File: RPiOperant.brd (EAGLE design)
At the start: 136 x 94 mm, 69 parts, among them IC1 74LS14N, IC2 74LS14N, J2 POWER_JACK

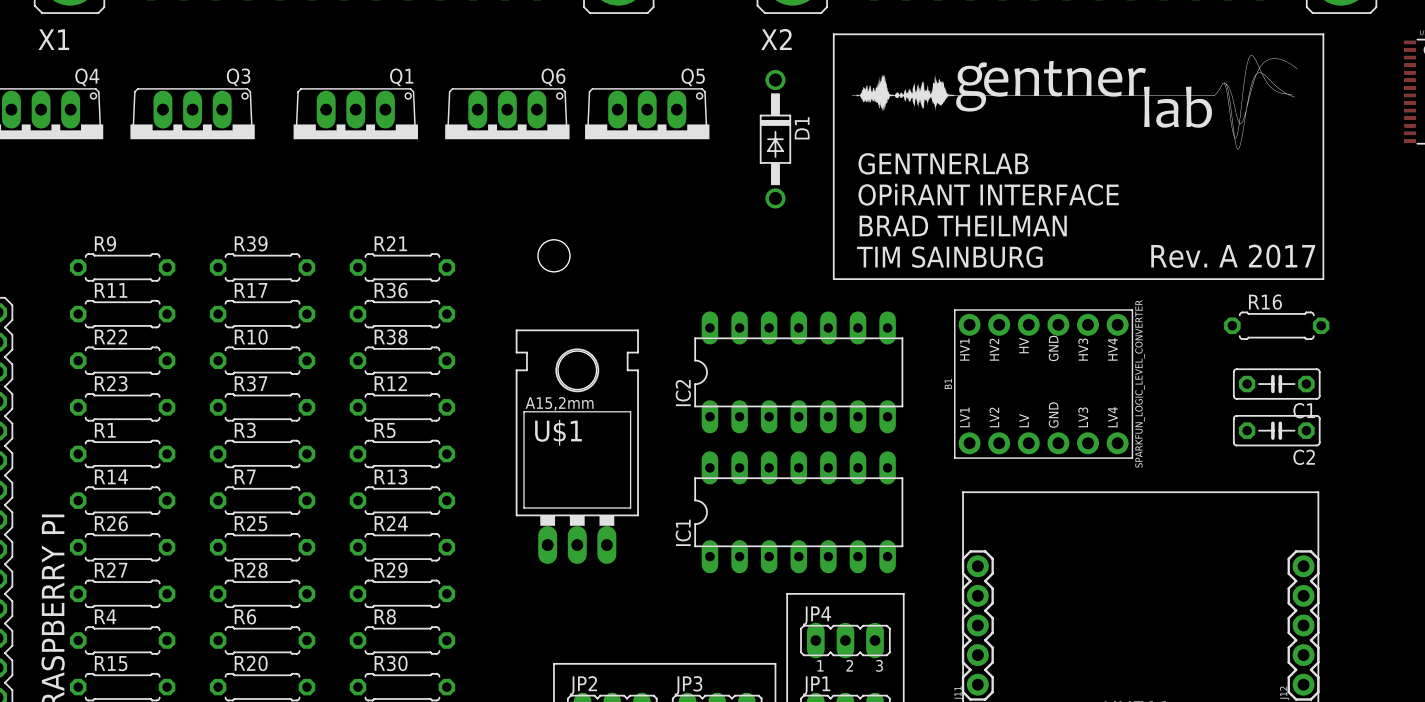
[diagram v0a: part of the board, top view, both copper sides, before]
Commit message: rev b changes... new DB25 pinout
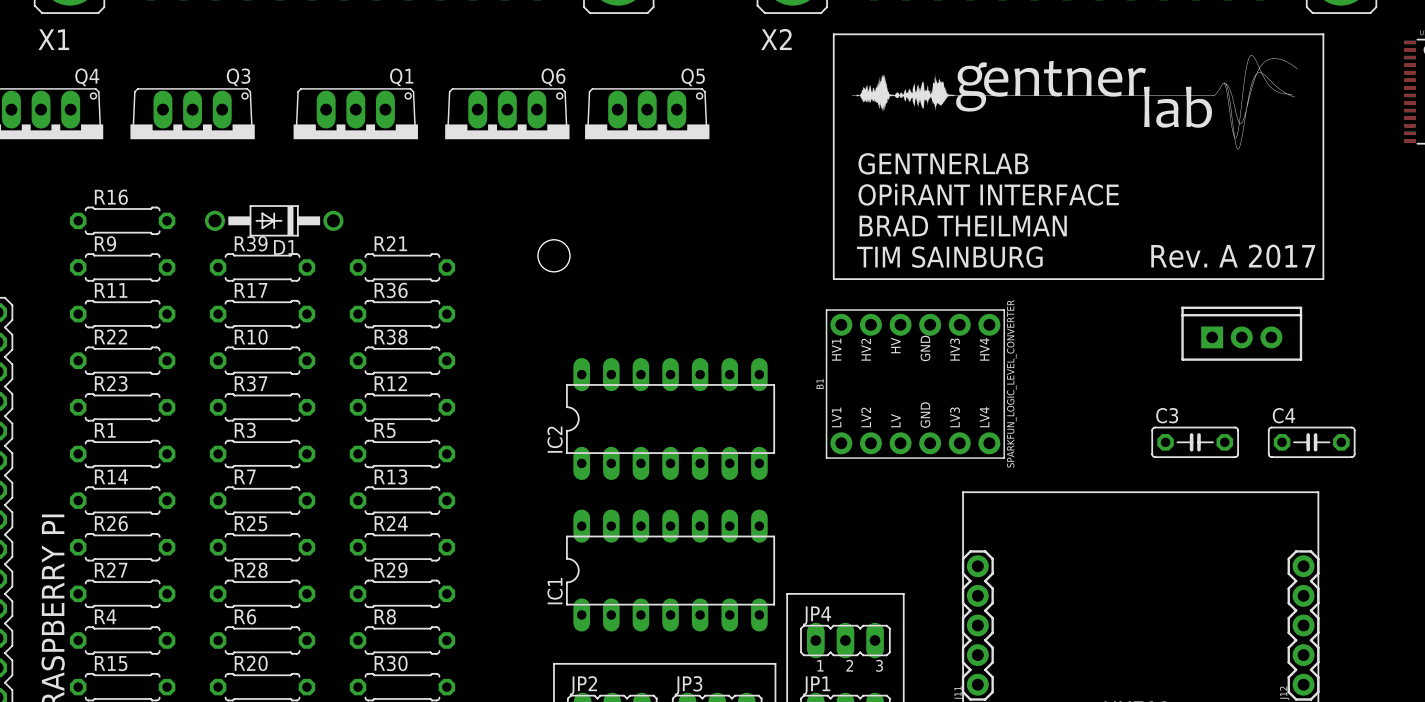
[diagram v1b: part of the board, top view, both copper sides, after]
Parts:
- removed C1: 100nF, adafruit:C050-025X075
- removed C2: 10uF, adafruit:C050-025X075
- removed U$1: V_REG_LD1117VXX, SparkFun-IC-Power:78XXL
- added C3: 100nF, adafruit:C050-025X075
- added C4: 10uF, adafruit:C050-025X075
- added U2: (no value), SparkFun-IC-Power:TO220-IGO
- moved R16 99.4 mm to (16.0, 65.0)
- moved D1 43.6 mm to (29.0, 65.0), turned to 180 degrees
- moved IC1 12.1 mm to (63.0, 35.0)
- moved IC2 11.7 mm to (63.0, 48.0)
- moved B1 11.0 mm to (84.0, 51.0)
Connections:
- net +3V3: now also C4.1, U2.OUT, X1.2; no longer C2.1, U$1.GND
- net 12V: now also C3.1, U2.IN, X1.1; no longer C1.1, U$1.OUT
- net GND: now also C3.2, C4.2, U2.GND; no longer C1.2, C2.2, U$1.IN
- net TTL22: no longer X1.2
- net TTL27: no longer X1.1

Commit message: new board layout
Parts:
- moved C4 107.7 mm to (14.0, 18.0), turned to 90 degrees
- moved C3 92.3 mm to (20.0, 18.0), turned to 90 degrees
- moved U2 85.0 mm to (36.0, 17.0)
- moved R1 79.0 mm to (95.0, 47.0)
- moved R10 79.0 mm to (107.0, 55.0)
- moved R11 79.0 mm to (95.0, 59.0)
- moved R12 79.0 mm to (119.0, 51.0)
- moved R13 79.0 mm to (119.0, 43.0)
- moved R14 79.0 mm to (95.0, 43.0)
- moved R15 79.0 mm to (95.0, 27.0)
- moved R17 79.0 mm to (107.0, 59.0)
- moved R2 79.0 mm to (95.0, 19.0)
- moved R20 79.0 mm to (107.0, 27.0)
- moved R21 79.0 mm to (119.0, 63.0)
- moved R22 79.0 mm to (95.0, 55.0)
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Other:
- board text added: "Rev. B 2018"
- board text removed: "3.3V 5V"
- board text removed: "5 V"
- board text removed: "GPIO LC"
- board text removed: "LOAD CELL SELECT"
- board text removed: "Rev. A 2017"
- board text removed: "TTL SELECT"

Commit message: revb revisions
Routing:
- net GND: track 0.00 -> 590.5 mm, vias 0 -> 6
- net 12V: track 0.00 -> 393.1 mm, vias 0 -> 4
- net +3V3: track 0.00 -> 347.9 mm, vias 0 -> 11
- net AUX2: track 0.00 -> 259.7 mm, vias 0 -> 9
- net GPIO7: track 0.00 -> 255.2 mm, vias 0 -> 2
- net RIGHT_PECK_GPIO: track 0.00 -> 243.1 mm, vias 0 -> 5
- net CENTER_PECK_GPIO: track 0.00 -> 233.9 mm, vias 0 -> 7
- net GPIO22: track 0.00 -> 223.7 mm, vias 0 -> 7
- net IR_5_GPIO: track 0.00 -> 221.8 mm, vias 0 -> 3
- net TXD: track 0.00 -> 213.0 mm, vias 0 -> 16
- net RXD: track 0.00 -> 207.8 mm, vias 0 -> 3
- net LEFT_PECK_GPIO: track 0.00 -> 199.9 mm, vias 0 -> 5
- net RPI_3.3V: track 0.00 -> 197.2 mm, vias 0 -> 7
- net HOPPER_IR_GPIO: track 0.00 -> 196.0 mm, vias 0 -> 4
- net SCL: track 0.00 -> 195.5 mm, vias 0 -> 4
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
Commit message: new board!
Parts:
- removed J1: (no value), SparkFun-Connectors:SCREWTERMINAL-3.5MM-4
- removed J10, J13, J14: (no value), SparkFun-Connectors:SCREWTERMINAL-3.5MM-3
- removed J15, J9: (no value), SparkFun-Connectors:SCREWTERMINAL-3.5MM-2
- removed X2: (no value), con-subd:F25HP
- added X3: 2550-, con-3m:PAK100/2500-50
- X1: value (none) -> 2516-; device con-subd:F25HP -> con-3m:PAK100/2500-16
- moved X1 80.8 mm to (41.5, 5.50)
- moved C3 64.0 mm to (19.0, 82.0), turned to 180 degrees
- moved U2 63.8 mm to (10.5, 75.5), turned to 270 degrees
- moved R38 58.6 mm to (64.5, 76.5), turned to 270 degrees
- moved B1 54.8 mm to (98.0, 8.00)
- moved R36 51.6 mm to (70.5, 76.5), turned to 270 degrees
- moved R13 51.3 mm to (72.0, 22.5), turned to 90 degrees
- moved R16 49.9 mm to (32.0, 51.5)
- moved C4 49.8 mm to (19.0, 67.5), turned to 180 degrees
- moved R12 49.6 mm to (76.5, 76.5), turned to 270 degrees
- moved R37 47.0 mm to (67.5, 76.5), turned to 270 degrees
- moved D1 44.8 mm to (33.0, 57.0), turned to 0 degrees
- moved J7 44.5 mm to (76.5, 3.00)
- moved J8 44.5 mm to (87.5, 3.00)
- moved R5 44.0 mm to (75.0, 46.5), turned to 270 degrees
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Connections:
- removed net N$32: J13.1, JP1.1
- removed net N$33: J13.2, JP4.1
- new net GPIO17EXT: JP1.1, X1.9
- new net GPIO8EXT: JP4.1, X1.10
- new net RGB_CUE_B\: X3.4
- net +3V3: now also X3.2; no longer X1.2
- net 12V: now also X3.1, X3.23; no longer X1.1, X1.23
- net AUX1: now also X1.1, X3.26; no longer J9.1, X2.1
- net AUX2: now also X1.2, X3.27; no longer J9.2, X2.2
- net AUX3: now also X1.3, X3.28; no longer J15.1, X2.3
- net AUX4: now also X1.4, X3.29; no longer J15.2, X2.4
- net AUX5: now also X1.5, X3.30; no longer J1.1, X2.5
- net AUX6: now also X1.6, X3.31; no longer J1.2, X2.6
- net AUX7: now also X1.7, X3.32; no longer J1.3, X2.7
- net AUX8: now also X1.8, X3.39; no longer J1.4, X2.14
- net CENTER_IR: now also X3.11; no longer X1.11
- net CENTER_LED: now also X3.8; no longer X1.8
- net GND: now also X1.15, X1.16; no longer J10.3, J13.3, J14.3, X1.G1, X1.G2, X2.G1, X2.G2
- net HOPPER: now also X3.6; no longer X1.6
- net HOPPER_IR: now also X3.13; no longer X1.13
- net HOUSELIGHT_B: now also X3.20; no longer X1.20
- net HOUSELIGHT_G: now also X3.21; no longer X1.21
- net HOUSELIGHT_R: now also X3.22; no longer X1.22
- net HOUSELIGHT_W: now also X3.19; no longer X1.19
- net IR_1: now also X3.50; no longer X2.25
- net IR_2: now also X3.49; no longer X2.24
- net IR_3: now also X3.48; no longer X2.23
- net IR_4: now also X3.47; no longer X2.22
- net IR_5: now also X3.46; no longer X2.21
- net IR_6: now also X3.45; no longer X2.20
- net LED_1: now also X3.38; no longer X2.13
- net LED_2: now also X3.37; no longer X2.12
- net LED_3: now also X3.36; no longer X2.11
- net LED_4: now also X3.35; no longer X2.10
- net LED_5: now also X3.34; no longer X2.9
- net LED_6: now also X3.33; no longer X2.8
- net LEFT_IR: now also X3.12; no longer X1.12
- net LEFT_LED: now also X3.9; no longer X1.9
- net LOADCELL2A+: now also X3.41; no longer X2.16
- net LOADCELL2A-: now also X3.40; no longer X2.15
- net LOADCELLA+: now also X3.15; no longer X1.15
- net LOADCELLA-: now also X3.14; no longer X1.14
- net LOADCELLE+: now also X3.25; no longer X1.25
- net LOADCELLE-: now also X3.24; no longer X1.24
- net RGB_CUE_B: no longer X1.4
- net RGB_CUE_G: now also X3.3; no longer X1.3
- net RGB_CUE_R: now also X3.5; no longer X1.5
- net RIGHT_IR: now also X3.10; no longer X1.10
- net RIGHT_LED: now also X3.7; no longer X1.7
- net RXD: now also X1.14; no longer J14.2
- net TTL22: now also X1.12; no longer J10.2
- net TTL27: now also X1.11; no longer J10.1
- net TXD: now also X1.13; no longer J14.1
- net USB1_D+: now also X3.16; no longer X1.16
- net USB1_D-: now also X3.17; no longer X1.17
- net USB1_VBUS: now also X3.18; no longer X1.18
- net USB2_D+: now also X3.42; no longer X2.17
- net USB2_D-: now also X3.43; no longer X2.18
- net USB2_VBUS: now also X3.44; no longer X2.19
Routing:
- net 12V: track 393.1 -> 165.0 mm, vias 4 -> 2
- net PCM_CLK: track 0.00 -> 168.9 mm, vias 0 -> 5
- net ID_SD: track 0.00 -> 149.3 mm, vias 0 -> 6
- net GPIO27: track 71.8 -> 201.3 mm, vias 2 -> 13
- net PCM_DIN: track 0.00 -> 128.8 mm, vias 0 -> 7
- net PCM_DOUT: track 0.00 -> 115.3 mm, vias 0 -> 2
- net GND: track 590.5 -> 475.2 mm, vias 6 -> 13
- net CENTER_PECK_GPIO: track 233.9 -> 132.7 mm, vias 7 -> 9
- net RXD: track 207.8 -> 308.8 mm, vias 3 -> 6
- net GPIO7: track 255.2 -> 161.4 mm, vias 2 -> 5
- net RGB_CUE_B: track 91.1 -> 0.00 mm, vias 3 -> 0
- net N$3: track 94.3 -> 5.09 mm, vias 2 -> 0
- net N$32: track 87.2 -> 0.00 mm, vias 3 -> 0
- net IR_3_GPIO: track 170.4 -> 251.6 mm, vias 9 -> 10
- net IR_5_GPIO: track 221.8 -> 140.6 mm, vias 3 -> 7
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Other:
- board size 136 x 94 mm -> 120 x 94 mm
- board text added: "+3.3V REGULATOR"
- board text added: "B"
- board text added: "Front Panel AUX"
- board text added: "G"
- board text added: "HOPPER"
- board text added: "HOUSELIGHTS"
- board text added: "IR Sensors"
- board text added: "LC SELECT EX LC"
- board text added: "LED CONTROL"
- board text added: "PCA9685"
- board text added: "PyOperant Interface Brad Theilman Tim Sainburg"
- board text added: "R"
- board text added: "TTL SELECT 3.3 5"
- board text added: "W"
- board text removed: "AUX1"
- board text removed: "AUX2"
- board text removed: "AUX3"
- board text removed: "AUX4"
- board text removed: "AUX5"
- board text removed: "AUX6"
- board text removed: "AUX7"
- board text removed: "AUX8"
- board text removed: "GENTNERLAB OPiRANT INTERFACE BRAD THEILMAN TIM SAINBURG"
- board text removed: "GND"
- board text removed: "GPIO17"
- board text removed: "GPIO8"
- board text removed: "RXD"
- board text removed: "TTL22"
- board text removed: "TTL27"
- board text removed: "TXD"

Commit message: new board
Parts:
- moved JP3 35.6 mm to (31.0, 43.5), turned to 90 degrees
- moved JP2 35.5 mm to (26.0, 43.5), turned to 90 degrees
- moved B1 31.4 mm to (67.5, 15.5)
- moved J11 25.8 mm to (50.0, 19.0), turned to 180 degrees
- moved J12 16.3 mm to (50.0, 46.9), turned to 180 degrees
- moved IC1 9.22 mm to (70.0, 41.0)
- moved IC2 9.22 mm to (90.5, 41.0)
- moved R1 9.22 mm to (62.0, 52.5)
- moved R13 9.22 mm to (65.0, 28.5)
- moved R14 9.22 mm to (68.0, 28.5)
- moved R15 9.22 mm to (74.0, 28.5)
- moved R2 9.22 mm to (77.0, 52.5)
- moved R20 9.22 mm to (71.0, 28.5)
- moved R24 9.22 mm to (82.5, 52.5)
- moved R25 9.22 mm to (85.5, 52.5)
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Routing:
- net RXD: track 308.8 -> 148.5 mm
- net LEFT_PECK_GPIO: track 203.8 -> 133.7 mm, vias 13 -> 6
- net IR_3_GPIO: track 251.6 -> 183.5 mm, vias 10 -> 6
- net GPIO27: track 201.3 -> 139.4 mm, vias 13 -> 5
- net USB1_D+: track 173.2 -> 116.9 mm, vias 4 -> 3
- net IR_6: track 138.8 -> 84.1 mm
- net HOUSELIGHT_B_GPIO: track 81.8 -> 130.1 mm, vias 5 -> 2
- net TTL22: track 12.5 -> 56.0 mm
- net IR_4_GPIO: track 134.5 -> 177.4 mm
- net AUX2: track 283.5 -> 243.6 mm, vias 6 -> 5
- net RPI_5V: track 193.7 -> 154.6 mm, vias 7 -> 5
- net GPIO22: track 191.3 -> 155.8 mm, vias 12 -> 4
- net AUX1: track 159.3 -> 124.5 mm
- net SCL: track 182.9 -> 148.9 mm, vias 5 -> 4
- net HOPPER_IR_GPIO: track 177.1 -> 144.3 mm, vias 8 -> 5
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
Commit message: rev_b layout
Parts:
- added R18, R19: 330, resistor:0207/7
- added X2: 22-23-2041, con-molex:22-23-2041
- moved C4 11.0 mm to (19.0, 78.5)
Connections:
- new net N$25: R19.1, X2.2
- new net N$31: R18.1, X2.3
- net +3V3: now also R19.2
- net GND: now also X2.1, X2.4
- net RPI_3.3V: now also R18.2
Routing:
- net USB1_D-: track 112.3 -> 218.9 mm, vias 7 -> 4
- net ID_SC: track 145.9 -> 234.8 mm, vias 6 -> 2
- net PCM_CLK: track 199.1 -> 111.9 mm, vias 2 -> 4
- net IR_1: track 93.4 -> 173.0 mm
- net GPIO27: track 139.4 -> 217.8 mm, vias 5 -> 3
- net USB1_D+: track 116.9 -> 189.9 mm
- net LOADCELLE+: track 78.7 -> 131.6 mm, vias 3 -> 2
- net IR_5_GPIO: track 171.9 -> 126.3 mm, vias 2 -> 4
- net GND: track 488.8 -> 443.3 mm, vias 9 -> 3
- net PCM_DOUT: track 142.9 -> 99.1 mm, vias 5 -> 0
- net IR_4_GPIO: track 177.4 -> 134.2 mm, vias 6 -> 4
- net IR_3_GPIO: track 183.5 -> 140.6 mm, vias 6 -> 4
- net USB1_VBUS: track 158.5 -> 118.8 mm, vias 4 -> 8
- net SDA: track 177.9 -> 139.1 mm, vias 2 -> 7
- net AUX2: track 243.6 -> 207.8 mm, vias 5 -> 6
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
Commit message: revb
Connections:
- removed net CENTNER_LED: R36.1
- removed net RGB_CUE_B\: X3.4
- net CENTER_LED: now also R36.1
- net RGB_CUE_B: now also X3.4
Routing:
- net ID_SC: track 234.8 -> 118.8 mm, vias 2 -> 3
- net USB1_D-: track 218.9 -> 118.6 mm
- net IR_1: track 173.0 -> 96.0 mm
- net USB1_D+: track 189.9 -> 113.8 mm, vias 3 -> 6
- net IR_6_GPIO: track 116.3 -> 190.8 mm
- net GND: track 443.3 -> 510.3 mm, vias 3 -> 7
- net RGB_CUE_B: track 0.00 -> 64.3 mm, vias 0 -> 2
- net AUX5: track 178.1 -> 116.0 mm, vias 1 -> 6
- net LOADCELLE-: track 90.4 -> 147.3 mm, vias 4 -> 2
- net HOPPER_TRIG_GPIO: track 139.7 -> 193.0 mm, vias 5 -> 3
- net AUX8: track 160.2 -> 109.7 mm, vias 6 -> 5
- net USB2_D-: track 140.5 -> 91.8 mm, vias 1 -> 5
- net GPIO4: track 108.2 -> 152.0 mm, vias 3 -> 6
- net CENTER_PECK_GPIO: track 130.1 -> 173.3 mm, vias 8 -> 5
- net IR_4_GPIO: track 134.2 -> 176.7 mm, vias 4 -> 5
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
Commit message: rev_c v1
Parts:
- added C1: 100nF, adafruit:C050-025X075
- added C2: 10uF, adafruit:C050-025X075
- added U3: (no value), SparkFun-IC-Power:TO220-IGO
- moved X2 112.4 mm to (128.0, 87.5)
- moved J2 61.0 mm to (80.0, -4.50)
- moved Q5 41.7 mm to (90.5, 68.0)
- moved Q1 41.6 mm to (90.5, 56.5)
- moved Q3 41.5 mm to (90.5, 76.5)
- moved B1 41.0 mm to (108.5, 15.0)
- moved IC1 41.0 mm to (111.0, 40.5)
- moved IC2 41.0 mm to (131.5, 40.5)
- moved J7 41.0 mm to (117.5, 2.50)
- moved J8 41.0 mm to (130.5, 2.50)
- moved R1 41.0 mm to (103.0, 52.0)
- moved R10 41.0 mm to (121.0, 76.0)
- moved R11 41.0 mm to (118.0, 76.0)
- moved R12 41.0 mm to (115.0, 76.0)
- moved R13 41.0 mm to (106.0, 28.0)
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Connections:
- new net 24V: C1.1, C3.1, J2.PWR, U2.IN, U3.IN, X3.1
- net 12V: now also C2.1, U3.OUT; no longer C3.1, J2.PWR, U2.IN, X3.1
- net GND: now also C1.2, C2.2, U3.GND
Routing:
- net GND: track 510.3 -> 0.00 mm, vias 7 -> 0
- net +3V3: track 251.2 -> 0.00 mm, vias 1 -> 0
- net RPI_3.3V: track 231.9 -> 0.00 mm, vias 8 -> 0
- net AUX2: track 194.3 -> 0.00 mm, vias 5 -> 0
- net HOPPER_TRIG_GPIO: track 193.0 -> 0.00 mm, vias 3 -> 0
- net IR_6_GPIO: track 190.8 -> 0.00 mm, vias 4 -> 0
- net TXD: track 182.7 -> 0.00 mm, vias 5 -> 0
- net RPI_5V: track 181.7 -> 0.00 mm, vias 5 -> 0
- net GPIO27: track 177.9 -> 0.00 mm, vias 6 -> 0
- net IR_4_GPIO: track 176.7 -> 0.00 mm, vias 5 -> 0
- net SCL: track 175.3 -> 0.00 mm, vias 2 -> 0
- net CENTER_PECK_GPIO: track 173.3 -> 0.00 mm, vias 5 -> 0
- net RXD: track 169.1 -> 0.00 mm, vias 6 -> 0
- net 12V: track 163.3 -> 0.00 mm, vias 5 -> 0
- net GPIO17: track 159.0 -> 0.00 mm, vias 5 -> 0
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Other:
- board size 120 x 94 mm -> 161 x 94.5 mm
- board text added: "+12V REGULATOR"
